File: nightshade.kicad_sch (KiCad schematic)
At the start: 102 parts, among them J1 Conn_02x13_Odd_Even, J2 Bus_ISA_16bit, J3 DB15_Female_HighDensity_Mount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, U1 GD542x_ISA, U2 SOJ_256Kx16, U3 SOJ_256Kx16, U4 LM334SM, U5 27C010, U6 'LS/ALS/F244, Y1 14.31818MHz

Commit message: Add files via upload
Updated to Version 0.8
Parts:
- removed C40: 0.1u, Capacitor_SMD:C_0805_2012Metric, symbol Device:C_Small
- removed R20, R21: 6.8K, Resistor_SMD:R_0603_1608Metric, symbol Device:R_Small
- added C51, C52, C53, C54, C55, C56: 0.1u, Capacitor_SMD:C_0805_2012Metric, symbol Device:C_Small
- added U7, U8: SOJ_256Kx16, SOJ_DRAM:SOJ-40_10.16x26.44mm_P1.27mm, symbol SOJ_DRAM:SOJ_256Kx16
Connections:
- net CAS0: now also U7.29 (~{LCAS})
- net CAS1: now also U7.28 (~{UCAS})
- net CAS2: now also U8.29 (~{LCAS})
- net CAS3: now also U8.28 (~{UCAS})
- net GND: now also JP1.1 (A), JP2.1 (A), C51.1, C52.1, C53.1, C54.1, C55.1, C56.1, U7.21 (GND), U7.27 (~{OE}), U7.35 (GND), U7.40 (GND), U8.21 (GND), U8.27 (~{OE}), U8.35 (GND), U8.40 (GND)
- net MA0: now also U7.16 (A0), U8.16 (A0)
- net MA1: now also U7.17 (A1), U8.17 (A1)
- net MA2: now also U7.18 (A2), U8.18 (A2)
- net MA3: now also U7.19 (A3), U8.19 (A3)
- net MA4: now also U7.22 (A4), U8.22 (A4)
- net MA5: now also U7.23 (A5), U8.23 (A5)
- net MA6: now also U7.24 (A6), U8.24 (A6)
- net MA7: now also U7.25 (A7), U8.25 (A7)
- net MA8: now also U7.26 (A8), U8.26 (A8)
- net MD0: now also U7.2 (IO1)
- net MD1: now also U7.3 (IO2)
- net MD10: now also U7.33 (IO11)
- net MD11: now also U7.34 (IO12)
- net MD12: now also U7.36 (IO13)
- net MD13: now also U7.37 (IO14)
- net MD14: now also U7.38 (IO15)
- net MD15: now also U7.39 (IO16)
- net MD16: now also U8.2 (IO1)
- net MD17: now also U8.3 (IO2)
- net MD18: now also U8.4 (IO3)
- net MD19: now also U8.5 (IO4)
- net MD2: now also U7.4 (IO3)
- net MD20: now also U8.7 (IO5)
- net MD21: now also U8.8 (IO6)
- net MD22: now also U8.9 (IO7)
- net MD23: now also U8.10 (IO8)
- net MD24: now also U8.31 (IO9)
- net MD25: now also U8.32 (IO10)
- net MD26: now also U8.33 (IO11)
- net MD27: now also U8.34 (IO12)
- net MD28: now also U8.36 (IO13)
- net MD29: now also U8.37 (IO14)
- net MD3: now also U7.5 (IO4)
- net MD30: now also U8.38 (IO15)
- net MD31: now also U8.39 (IO16)
- net MD4: now also U7.7 (IO5)
- net MD5: now also U7.8 (IO6)
- net MD6: now also U7.9 (IO7)
- net MD7: now also U7.10 (IO8)
- net MD8: now also U7.31 (IO9)
- net MD9: now also U7.32 (IO10)
- net RAS1: now also U7.14 (~{RAS}), U8.14 (~{RAS})
- net VCC: now also C51.2, C52.2, C53.2, C54.2, C55.2, C56.2, U7.1 (Vcc), U7.20 (Vcc), U7.6 (Vcc), U8.1 (Vcc), U8.20 (Vcc), U8.6 (Vcc)
- net WE: now also U7.13 (~{WE}), U8.13 (~{WE})
- no-connect marks 44 -> 43
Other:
- note added: "1ST MEG: WHAT GETS IT DONE"
- note added: "2ND MEG: WORSE THAN USELESS"
- note removed: "EVIL!"
- note removed: "THANKS FOR THE MEMORIES..."
- moved on the sheet: C1, C10, C11, C12, C13, C14, C15, C16, C17, C18, C19, C2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

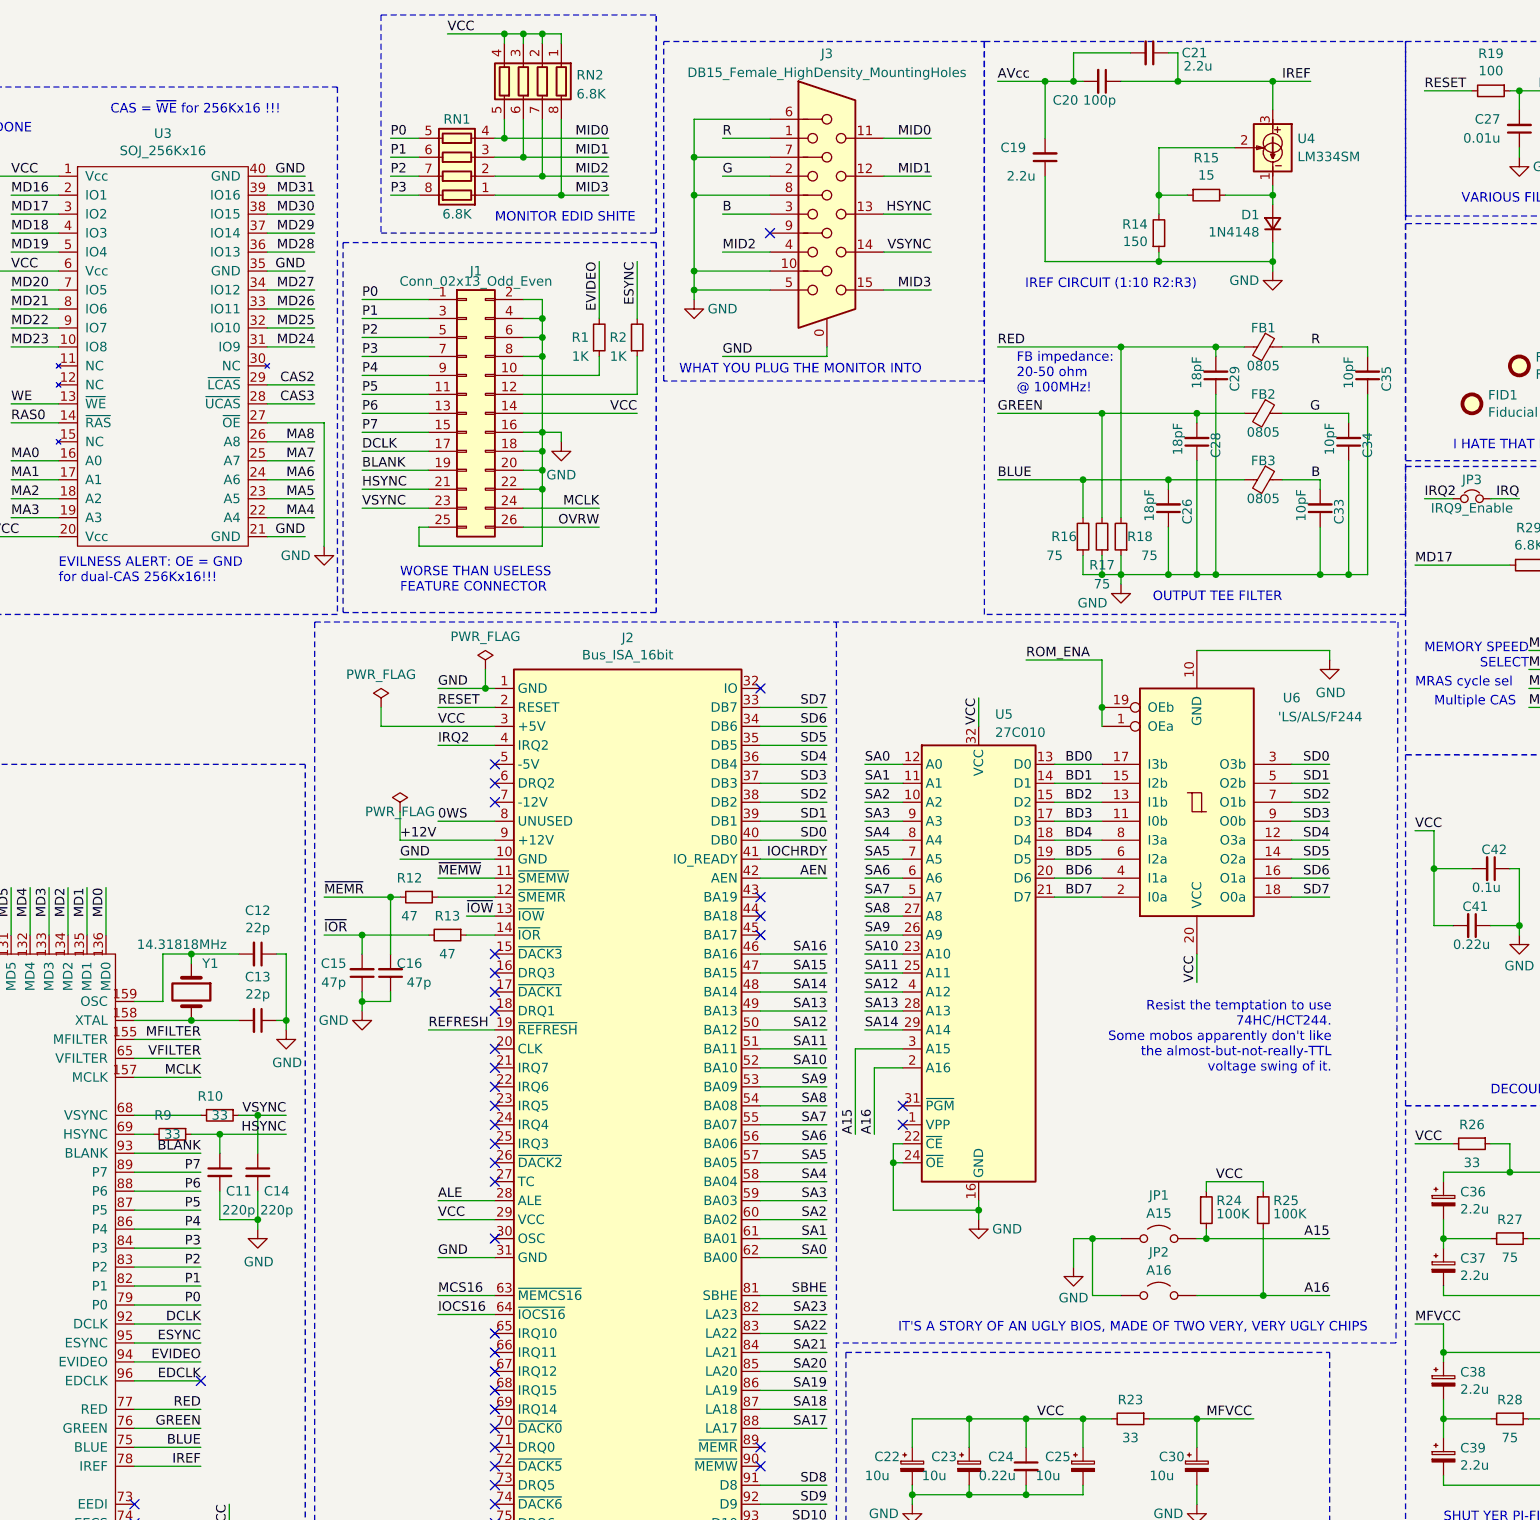
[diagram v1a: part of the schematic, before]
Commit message: Add files via upload
Uploaded version 0.8a, which fixes among other things the VFC connector pinout.
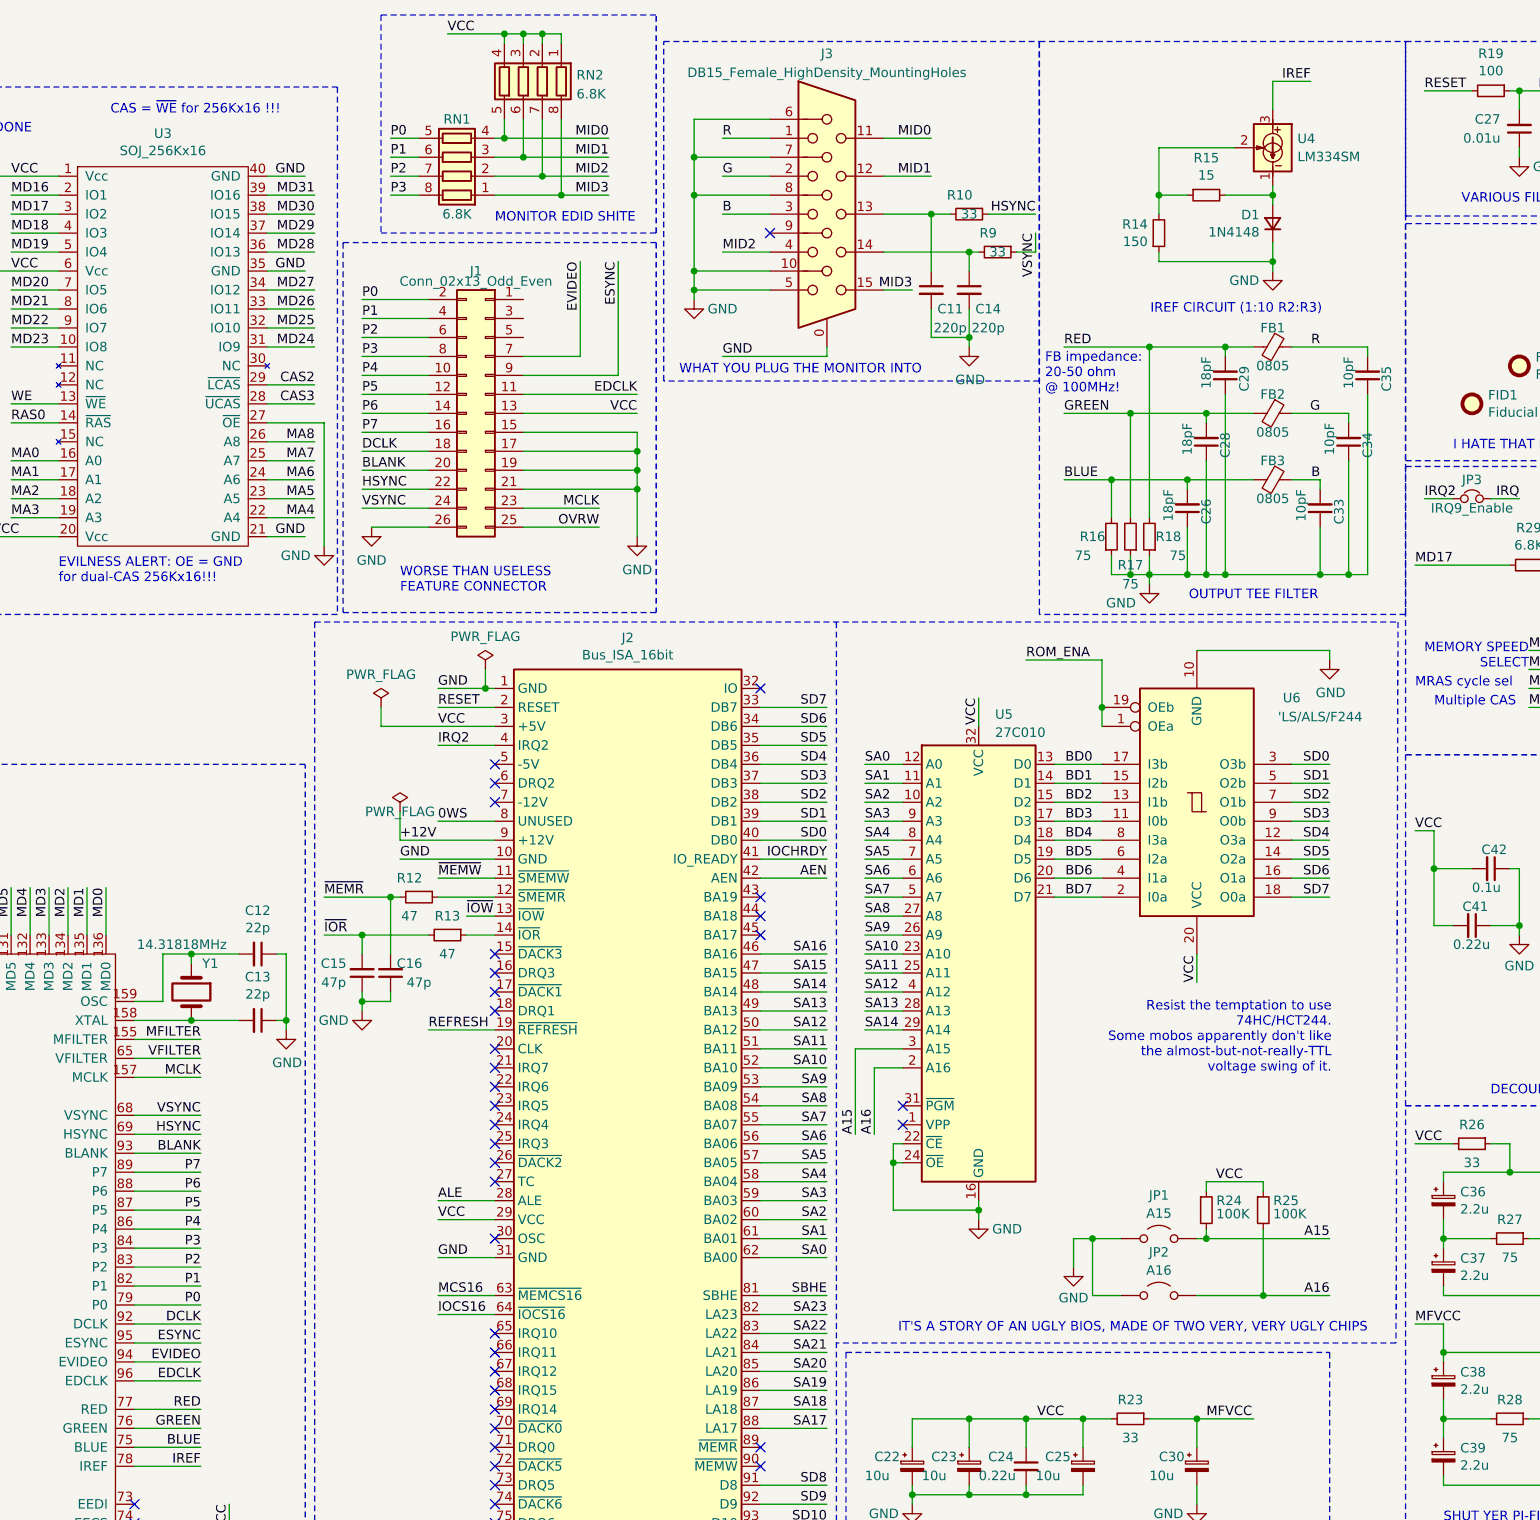
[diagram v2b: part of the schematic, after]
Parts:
- removed C19, C21: 2.2u, Capacitor_SMD:C_0805_2012Metric, symbol Device:C_Small
- removed C20: 100p, Capacitor_SMD:C_0805_2012Metric, symbol Device:C_Small
- removed R1, R2: 1K, Resistor_SMD:R_0805_2012Metric, symbol Device:R_Small
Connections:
- net BLANK: now also J1.20 (Pin_20); no longer J1.19 (Pin_19)
- net DCLK: now also J1.18 (Pin_18); no longer J1.17 (Pin_17)
- net EDCLK: now also J1.11 (Pin_11)
- net ESYNC: now also J1.9 (Pin_9)
- net EVIDEO: now also J1.7 (Pin_7)
- net GND: now also J1.15 (Pin_15), J1.17 (Pin_17), J1.19 (Pin_19), J1.21 (Pin_21), J1.26 (Pin_26); no longer J1.16 (Pin_16), J1.18 (Pin_18), J1.2 (Pin_2), J1.20 (Pin_20), J1.22 (Pin_22), J1.25 (Pin_25), J1.4 (Pin_4), J1.6 (Pin_6), J1.8 (Pin_8)
- net HSYNC: now also J1.22 (Pin_22), R10.1, U1.69 (HSYNC); no longer C11.1, J1.21 (Pin_21), J3.13, R9.1
- net MCLK: now also J1.23 (Pin_23); no longer J1.24 (Pin_24)
- net OVRW: now also J1.25 (Pin_25); no longer J1.26 (Pin_26)
- net P0: now also J1.2 (Pin_2); no longer J1.1 (Pin_1)
- net P1: now also J1.4 (Pin_4); no longer J1.3 (Pin_3)
- net P2: now also J1.6 (Pin_6); no longer J1.5 (Pin_5)
- net P3: now also J1.8 (Pin_8); no longer J1.7 (Pin_7)
- net P4: now also J1.10 (Pin_10); no longer J1.9 (Pin_9)
- net P5: now also J1.12 (Pin_12); no longer J1.11 (Pin_11)
- net P6: now also J1.14 (Pin_14); no longer J1.13 (Pin_13)
- net P7: now also J1.16 (Pin_16); no longer J1.15 (Pin_15)
- net VCC: now also J1.13 (Pin_13); no longer J1.14 (Pin_14)
- net VSYNC: now also J1.24 (Pin_24), R9.1, U1.68 (VSYNC); no longer C14.1, J1.23 (Pin_23), J3.14, R10.1
- net at R10.2: now also C11.1, J3.13; no longer U1.68 (VSYNC)
- net at R9.2: now also C14.1, J3.14; no longer U1.69 (HSYNC)
- no-connect marks 43 -> 42
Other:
- moved on the sheet: C11, C14, C26, C28, C29, FB1, FB2, FB3, R10, R16, R17, R18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

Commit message: Add files via upload
Updated to version 0.8b. Merry Christmas!
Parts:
- removed C36, C38: 2.2u, Capacitor_SMD:C_0805_2012Metric, symbol nightshade-rescue:CP_Small-Device
- removed C43, C45: 0.22u, Capacitor_SMD:C_0805_2012Metric, symbol Device:C_Small
- removed C9: 0.1u, Capacitor_SMD:C_0805_2012Metric, symbol Device:C_Small
- removed R23, R26: 33, Resistor_SMD:R_0805_2012Metric, symbol Device:R_Small
- removed Y1: 14.31818MHz, Crystal:Crystal_SMD_HC49-SD, symbol Device:Crystal
- added FB4, FB5: 0805-HiZ, No Resonance, Inductor_SMD:L_0805_2012Metric, symbol Device:FerriteBead_Small
- added Y1: 14.31818MHz, Crystal:Crystal_SMD_5032-2Pin_5.0x3.2mm_HandSoldering, symbol Device:Crystal_Small
- C12, C13: value 22p -> C_Small
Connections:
- net GND: now also C12.2, C13.2, C37.1, C39.1, C42.2; no longer C12.1, C13.1, C37.2, C39.2, C42.1
- net MCLKVCC: now also FB5.2
- net VCC: now also C42.1, FB4.1, FB5.1; no longer C42.2
- net VCLKVCC: now also FB4.2
- net XTAL: now reaches U1.158 (XTAL)
- net XTAL: now also C13.1, Y1.2; no longer C13.2
- net OSC: now reaches U1.159 (OSC)
- net OSC: now also C12.1, Y1.1; no longer C12.2
- net at R27.2: now also C37.2; no longer C37.1
- net at R28.2: now also C39.2; no longer C39.1
- no-connect marks 42 -> 45
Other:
- note removed: "DECOUPLING"
- moved on the sheet: C22, C23, C24, C25, C30, C31, C37, C39, C41, C42, C44, C46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

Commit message: Add files via upload
Updated to 0.8b2
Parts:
- removed U4: LM334SM, Package_SO:SOIC-8_3.9x4.9mm_P1.27mm, symbol Reference_Current:LM334SM
- added U4: LM334M, Package_SO:SOIC-8_3.9x4.9mm_P1.27mm, symbol Reference_Current:LM334M
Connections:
- net IREF: now also U4.4
- net at D1.2 (A), R15.2: now also U4.2, U4.3, U4.6, U4.7
- net at R14.2, R15.1: now also U4.1
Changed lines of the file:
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@@
-	)
-	(symbol
-		(lib_id "Reference_Current:LM334SM")
-		(at 353.06 35.56 0)
-		(mirror y)
-		(unit 1)
-		(exclude_from_sim no)
-		(in_bom yes)
-		(on_board yes)
-		(dnp no)
-		(property "Reference" "U4"
-			(at 356.3619 34.3478 0)
-			(effects
-				(font
-					(size 1.27 1.27)
-				)
-				(justify right)
-			)
-		)
-		(property "Value" "LM334SM"
-			(at 356.3619 36.7721 0)
-			(effects
-				(font
-					(size 1.27 1.27)
-				)
-				(justify right)
-			)
-		)
-		(property "Footprint" "Package_SO:SOIC-8_3.9x4.9mm_P1.27mm"
-			(at 352.425 40.005 0)
-			(effects
-				(font
-					(size 1.27 1.27)
-					(italic yes)
-				)
-				(justify left)
-				(hide yes)
-			)
-		)
-		(property "Datasheet" "http://www.ti.com/lit/ds/symlink/lm134.pdf"
-			(at 353.06 35.56 0)
-			(effects
-				(font
-					(size 1.27 1.27)
-					(italic yes)
-				)
-				(hide yes)
-			)
-		)
-		(property "Description" "1μA to 10mA 3-Terminal Adjustable Current Source, SO-8 Alternate"
-			(at 353.06 35.56 0)
-			(effects
-				(font
-					(size 1.27 1.27)
-				)
-				(hide yes)
-			)
-		)
-		(pin "3"
-		)
-		(pin "2"
-		)
-		(pin "1"
-		)
-		(instances
-			(project ""
-				(path "/5b408b6b-bd13-41fb-8952-41472f553b2d"
-					(reference "U4")
-					(unit 1)
-				)
-			)
-		)
 	)
 	(symbol
@@
 					(unit 1)
 				)
+			)
+		)
+	)
+	(symbol
+		(lib_id "Reference_Current:LM334M")
+		(at 353.06 35.56 0)
+		(mirror y)
+		(unit 1)
+		(exclude_from_sim no)
+		(in_bom yes)
+		(on_board yes)
+		(dnp no)
+		(property "Reference" "U4"
+			(at 356.108 34.0303 0)
+			(effects
+				(font
+					(size 1.27 1.27)
+				)
+				(justify right)
+			)
+		)
+		(property "Value" "LM334M"
+			(at 356.108 36.4546 0)
+			(effects
+				(font
+					(size 1.27 1.27)
+				)
+				(justify right)
+			)
+		)
+		(property "Footprint" "Package_SO:SOIC-8_3.9x4.9mm_P1.27mm"
+			(at 352.425 39.37 0)
+			(effects
+				(font
+					(size 1.27 1.27)
+					(italic yes)
+				)
+				(justify left)
+				(hide yes)
+			)
+		)
+		(property "Datasheet" "http://www.ti.com/lit/ds/symlink/lm134.pdf"
+			(at 353.06 35.56 0)
+			(effects
+				(font
+					(size 1.27 1.27)
+					(italic yes)
+				)
+				(hide yes)
+			)
+		)
+		(property "Description" "1μA to 10mA 3-Terminal Adjustable Current Source, SO-8"
+			(at 353.06 35.56 0)
+			(effects
+				(font
+					(size 1.27 1.27)
+				)
+				(hide yes)
+			)
+		)
+		(pin "1"
+		)
+		(pin "3"
+		)
+		(pin "7"
+		)
+		(pin "6"
+		)
+		(pin "4"
+		)
+		(pin "2"
+		)
+		(instances
+			(project ""
+				(path "/5b408b6b-bd13-41fb-8952-41472f553b2d"
+					(reference "U4")
+					(unit 1)
+				)

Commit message: Add files via upload
Updated to version 0.8c.
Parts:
- added C9: 0.22u, Capacitor_SMD:C_0805_2012Metric, symbol Device:C_Small
- added U9: LF50_TO252, Package_TO_SOT_SMD:TO-252-2, symbol Regulator_Linear:LF50_TO252
- C12, C13: value C_Small -> 15p
- C31: value 0.22u -> 22u; footprint Capacitor_SMD:C_0805_2012Metric -> Capacitor_SMD:C_Elec_4x5.8
- C7, C8: value 0.1u -> 10u; footprint Capacitor_SMD:C_0805_2012Metric -> Capacitor_SMD:C_1206_3216Metric
- R22: now not fitted
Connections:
- net +12V: now also C9.2, U9.1 (VI)
- net AVcc: now also U9.3 (VO)
- net BD4: now also U6.2 (I0a); no longer U6.8 (I3a)
- net BD5: now also U6.4 (I1a); no longer U6.6 (I2a)
- net BD6: now also U6.6 (I2a); no longer U6.4 (I1a)
- net BD7: now also U6.8 (I3a); no longer U6.2 (I0a)
- net GND: now also C9.1, U9.2 (GND)
- net SD4: now also U6.18 (O0a); no longer U6.12 (O3a)
- net SD5: now also U6.16 (O1a); no longer U6.14 (O2a)
- net SD6: now also U6.14 (O2a); no longer U6.16 (O1a)
- net SD7: now also U6.12 (O3a); no longer U6.18 (O0a)
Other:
- note added: "Do NOT install R22 if using the regulator!!"
- moved on the sheet: C31, U6

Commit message: Add files via upload
updated to 0.8c1.
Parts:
- U5: footprint Package_LCC:PLCC-32_11.4x14.0mm_P1.27mm -> SOJ_DRAM:PLCC-32_SMD-Socket
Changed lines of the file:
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@@
 			)
 		)
-		(property "Footprint" "Package_LCC:PLCC-32_11.4x14.0mm_P1.27mm"
+		(property "Footprint" "SOJ_DRAM:PLCC-32_SMD-Socket"
 			(at 313.69 143.51 0)
 			(effects
